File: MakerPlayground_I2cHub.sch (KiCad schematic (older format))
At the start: 9 parts, among them J1 Conn_01x04, J2 Conn_01x04, J3 Conn_01x04, J4 Conn_01x04, J5 Conn_01x04

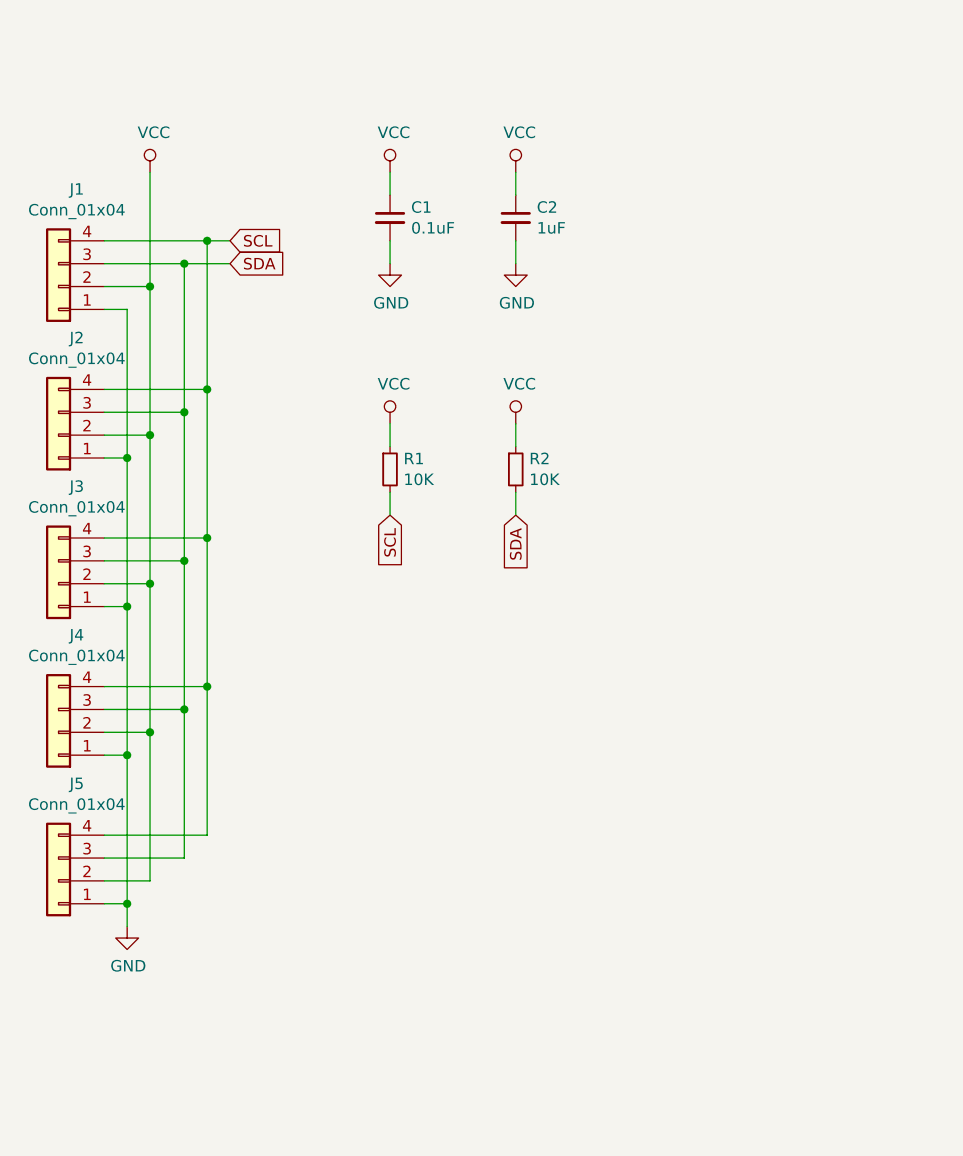
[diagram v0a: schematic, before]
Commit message: Add more capacitors & new capacitors, resistors alignment.
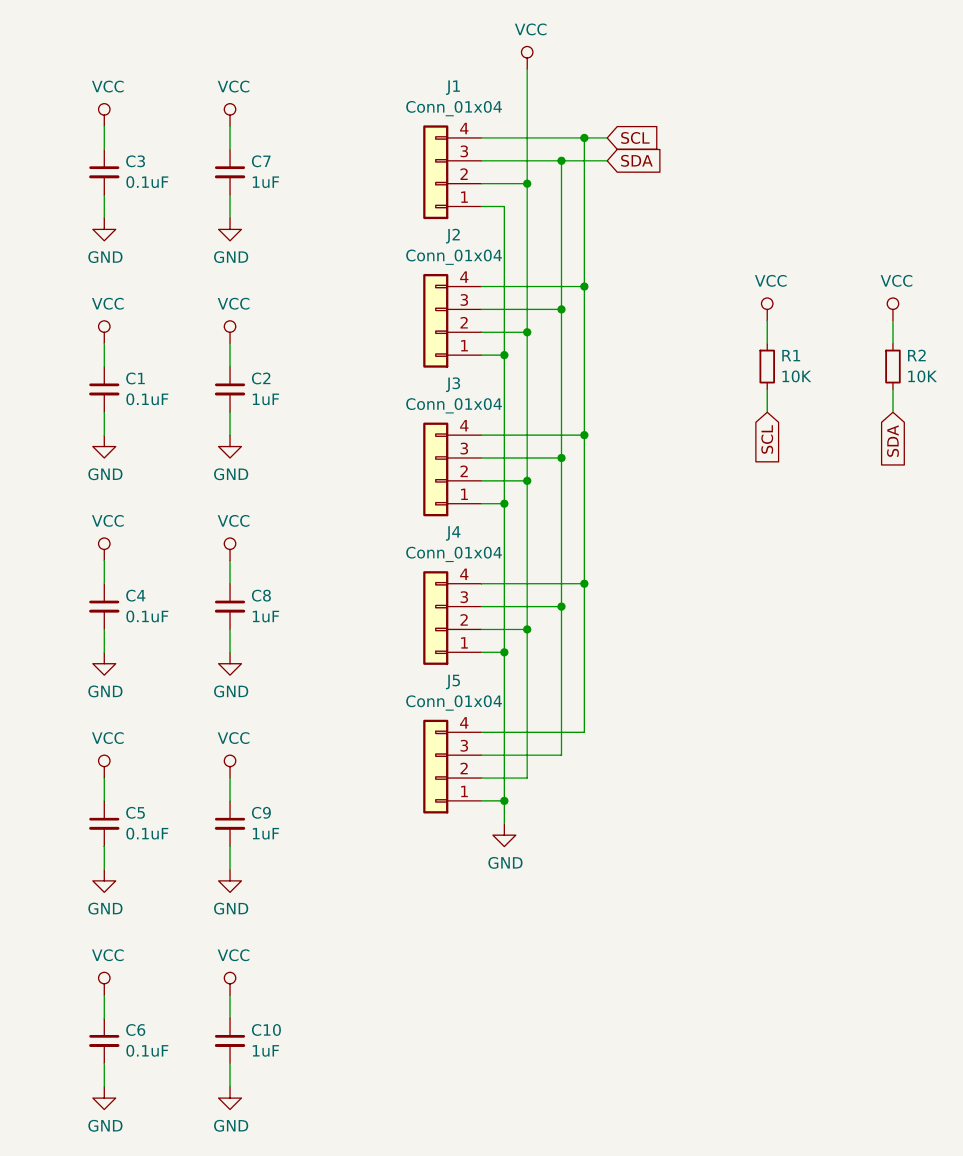
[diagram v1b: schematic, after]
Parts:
- added C10, C7, C8, C9: 1uF, Capacitor_SMD:C_0603_1608Metric, symbol Device:C_Small
- added C3, C4, C5, C6: 0.1uF, Capacitor_SMD:C_0603_1608Metric, symbol Device:C_Small
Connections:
- net GND: now also C10.2, C3.2, C4.2, C5.2, C6.2, C7.2, C8.2, C9.2
- net VCC: now also C10.1, C3.1, C4.1, C5.1, C6.1, C7.1, C8.1, C9.1
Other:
- moved on the sheet: C1, C2, J1, J2, J3, J4, J5, R1, R2
